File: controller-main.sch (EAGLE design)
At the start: 24 parts

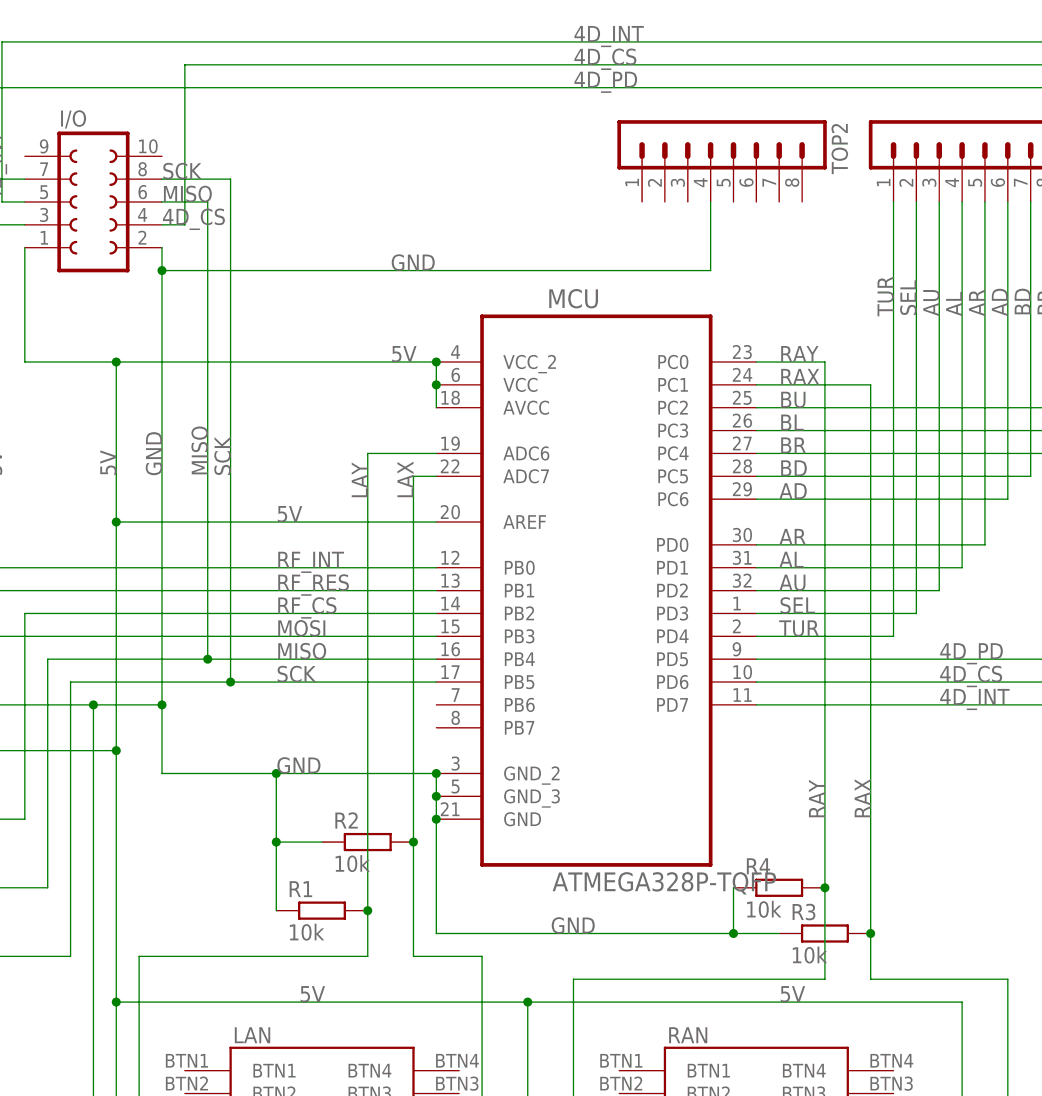
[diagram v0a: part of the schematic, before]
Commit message: Created basic main board desing
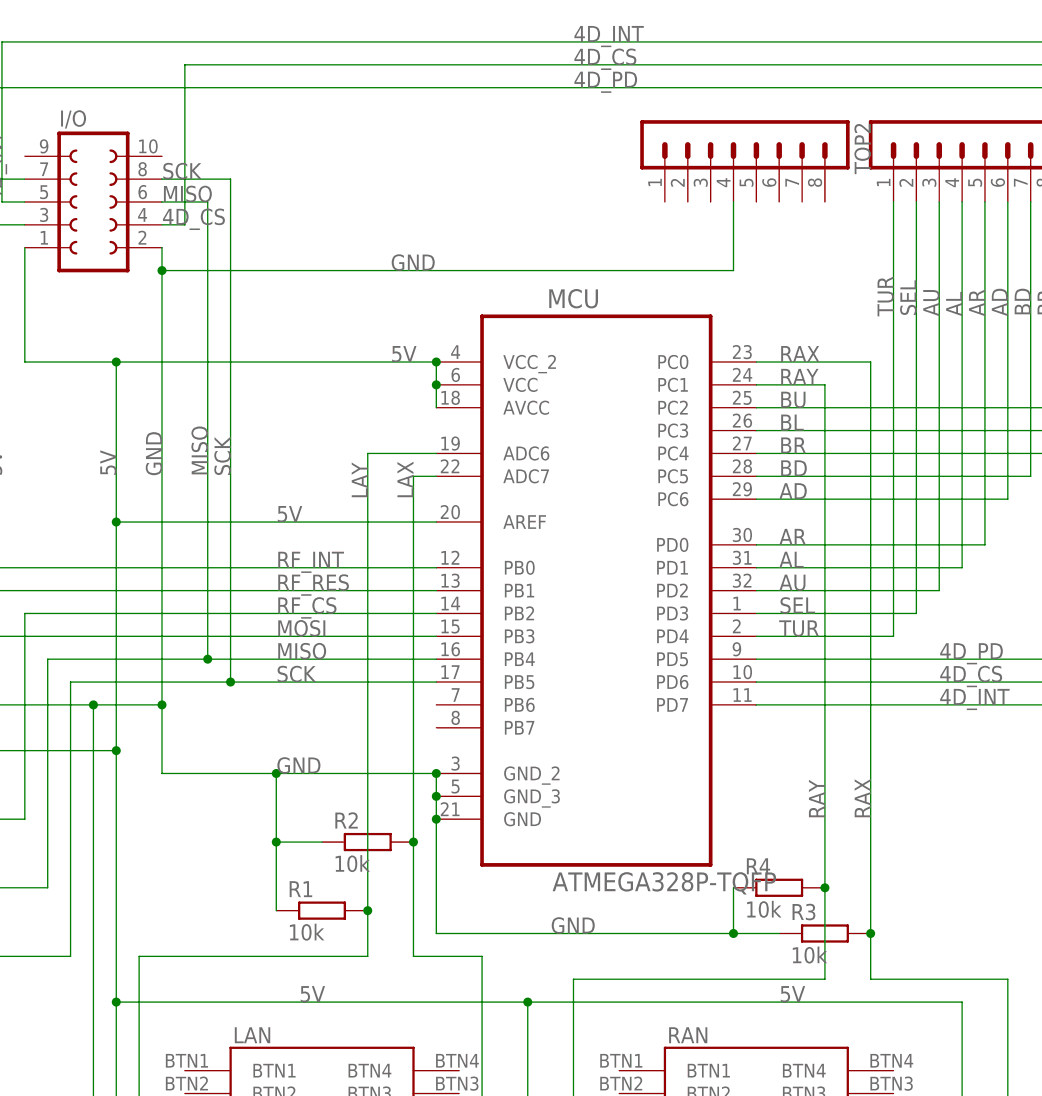
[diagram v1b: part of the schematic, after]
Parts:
- TOP2: device con-lstb:MA08-1 -> con-lstb:MA08-1W
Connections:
- net RAX: now also MCU.PC0; no longer MCU.PC1
- net RAY: now also MCU.PC1; no longer MCU.PC0
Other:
- moved on the sheet: TOP2
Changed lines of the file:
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@@
 <?xml version="1.0" encoding="utf-8"?>
 <!DOCTYPE eagle SYSTEM "eagle.dtd">
-<eagle version="8.4.0">
+<eagle version="8.4.1">
 <drawing>
 <settings>
@@
 <part name="I/O" library="con-lsta" library_urn="urn:adsk.eagle:library:161" deviceset="FE05-2W" device="" package3d_urn="urn:adsk.eagle:package:8205/1"/>
 <part name="TOP1" library="con-lstb" library_urn="urn:adsk.eagle:library:162" deviceset="MA10-1W" device="" package3d_urn="urn:adsk.eagle:package:8347/1"/>
-<part name="TOP2" library="con-lstb" library_urn="urn:adsk.eagle:library:162" deviceset="MA08-1" device="" package3d_urn="urn:adsk.eagle:package:8343/1"/>
 <part name="LAN" library="joystick" deviceset="JOYSTICK" device="JOYSTICKWBTN" value="JOYSTICK"/>
 <part name="RAN" library="joystick" deviceset="JOYSTICK" device="JOYSTICKWBTN" value="JOYSTICK"/>
@@
 <part name="R15" library="resistor" library_urn="urn:adsk.eagle:library:348" deviceset="R-EU_" device="M1206" package3d_urn="urn:adsk.eagle:package:26088/1" value="2k"/>
 <part name="R16" library="resistor" library_urn="urn:adsk.eagle:library:348" deviceset="R-EU_" device="M1206" package3d_urn="urn:adsk.eagle:package:26088/1" value="1k"/>
+<part name="TOP2" library="con-lstb" library_urn="urn:adsk.eagle:library:162" deviceset="MA08-1W" device="" package3d_urn="urn:adsk.eagle:package:8344/1"/>
 </parts>
 <sheets>
@@
 <instance part="I/O" gate="G$1" x="81.28" y="121.92"/>
 <instance part="TOP1" gate="1" x="180.34" y="129.54" rot="R270"/>
-<instance part="TOP2" gate="1" x="149.86" y="129.54" rot="R270"/>
 <instance part="LAN" gate="G$1" x="106.68" y="17.78"/>
 <instance part="RAN" gate="G$1" x="154.94" y="17.78"/>
@@
 <instance part="R15" gate="G$1" x="45.72" y="38.1"/>
 <instance part="R16" gate="G$1" x="55.88" y="38.1"/>
+<instance part="TOP2" gate="1" x="152.4" y="129.54" rot="R270"/>
 </instances>
 <busses>
@@
 <wire x1="88.9" y1="114.3" x2="88.9" y2="116.84" width="0.1524" layer="91"/>
 <junction x="88.9" y="66.04"/>
-<pinref part="TOP2" gate="1" pin="4"/>
 <wire x1="40.64" y1="66.04" x2="81.28" y2="66.04" width="0.1524" layer="91"/>
 <wire x1="81.28" y1="66.04" x2="88.9" y2="66.04" width="0.1524" layer="91"/>
-<wire x1="149.86" y1="121.92" x2="149.86" y2="114.3" width="0.1524" layer="91"/>
-<wire x1="149.86" y1="114.3" x2="88.9" y2="114.3" width="0.1524" layer="91"/>
 <junction x="88.9" y="114.3"/>
 <pinref part="LAN" gate="G$1" pin="GNDY"/>
+<wire x1="152.4" y1="114.3" x2="88.9" y2="114.3" width="0.1524" layer="91"/>
 <wire x1="81.28" y1="66.04" x2="81.28" y2="10.16" width="0.1524" layer="91"/>
 <wire x1="81.28" y1="10.16" x2="91.44" y2="10.16" width="0.1524" layer="91"/>
@@
 <wire x1="25.4" y1="60.96" x2="25.4" y2="58.42" width="0.1524" layer="91"/>
 <junction x="25.4" y="60.96"/>
+<pinref part="TOP2" gate="1" pin="4"/>
+<wire x1="152.4" y1="121.92" x2="152.4" y2="114.3" width="0.1524" layer="91"/>
 </segment>
 </net>
@@
 <net name="RAY" class="0">
 <segment>
-<pinref part="MCU" gate="A" pin="PC0"/>
-<wire x1="162.56" y1="104.14" x2="154.94" y2="104.14" width="0.1524" layer="91"/>
-<wire x1="162.56" y1="104.14" x2="162.56" y2="45.72" width="0.1524" layer="91"/>
+<wire x1="162.56" y1="101.6" x2="162.56" y2="45.72" width="0.1524" layer="91"/>
 <wire x1="134.62" y1="35.56" x2="162.56" y2="35.56" width="0.1524" layer="91"/>
 <pinref part="R4" gate="G$1" pin="2"/>
 <junction x="162.56" y="45.72"/>
-<label x="157.48" y="104.14" size="1.778" layer="95"/>
+<label x="157.48" y="101.6" size="1.778" layer="95"/>
 <label x="162.56" y="53.34" size="1.778" layer="95" rot="R90"/>
 <pinref part="RAN" gate="G$1" pin="OUTY"/>
@@
 <wire x1="134.62" y1="12.7" x2="134.62" y2="35.56" width="0.1524" layer="91"/>
 <wire x1="162.56" y1="35.56" x2="162.56" y2="45.72" width="0.1524" layer="91"/>
+<pinref part="MCU" gate="A" pin="PC1"/>
+<wire x1="154.94" y1="101.6" x2="162.56" y2="101.6" width="0.1524" layer="91"/>
 </segment>
 </net>
 <net name="RAX" class="0">
 <segment>
-<pinref part="MCU" gate="A" pin="PC1"/>
-<wire x1="154.94" y1="101.6" x2="167.64" y2="101.6" width="0.1524" layer="91"/>
-<wire x1="167.64" y1="101.6" x2="167.64" y2="40.64" width="0.1524" layer="91"/>
+<wire x1="167.64" y1="104.14" x2="167.64" y2="40.64" width="0.1524" layer="91"/>
 <pinref part="R3" gate="G$1" pin="2"/>
 <wire x1="167.64" y1="40.64" x2="167.64" y2="35.56" width="0.1524" layer="91"/>
@@
 <wire x1="182.88" y1="35.56" x2="182.88" y2="12.7" width="0.1524" layer="91"/>
 <wire x1="182.88" y1="12.7" x2="170.18" y2="12.7" width="0.1524" layer="91"/>
-<label x="157.48" y="101.6" size="1.778" layer="95"/>
+<label x="157.48" y="104.14" size="1.778" layer="95"/>
 <label x="167.64" y="53.34" size="1.778" layer="95" rot="R90"/>
-</segment>
-</net>
+<pinref part="MCU" gate="A" pin="PC0"/>
+<wire x1="154.94" y1="104.14" x2="167.64" y2="104.14" width="0.1524" layer="91"/>
+</segment>
+</net>

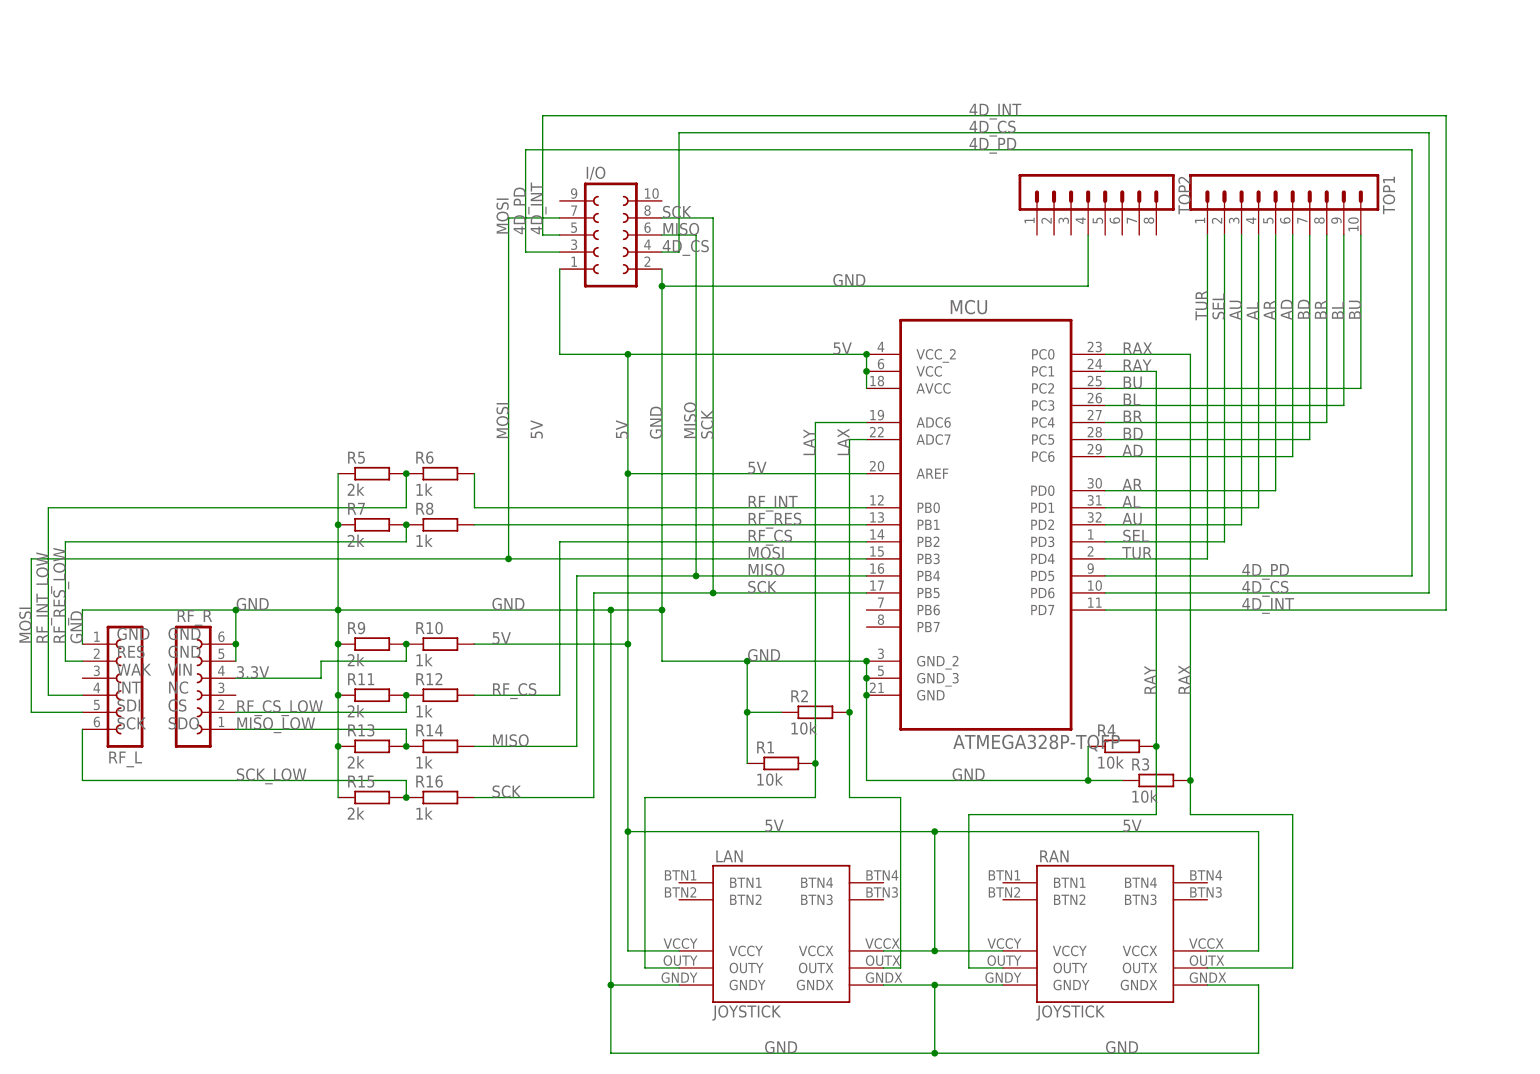
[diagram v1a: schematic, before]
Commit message: Changed pin connections on the main board
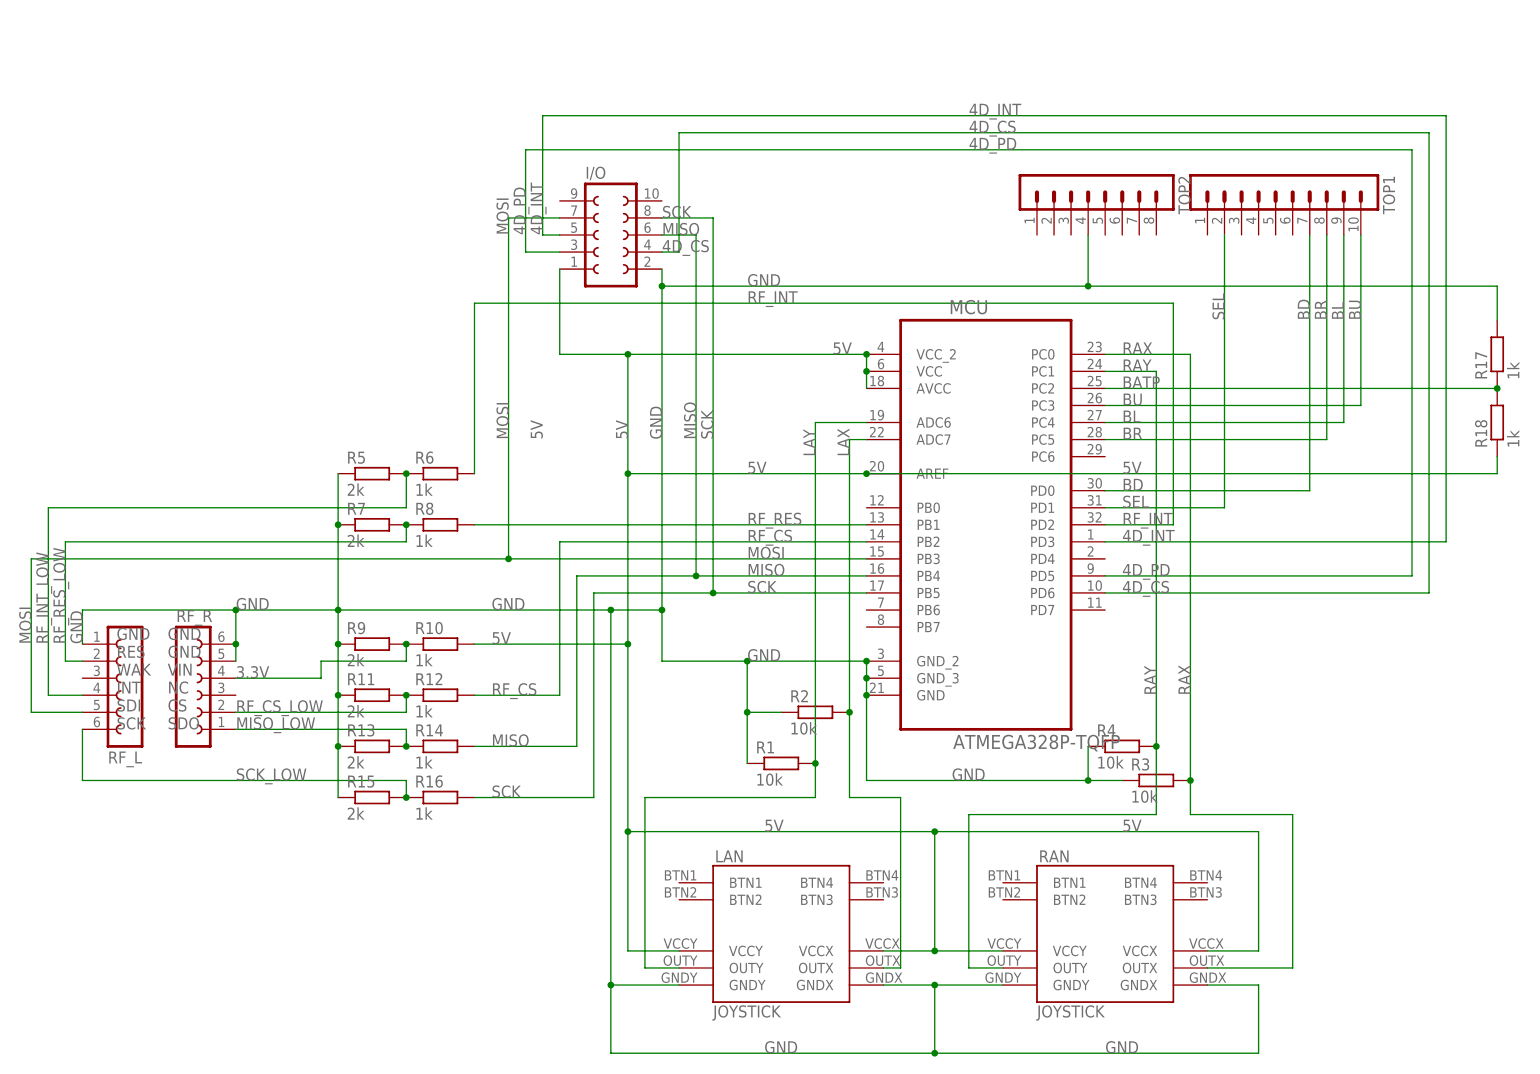
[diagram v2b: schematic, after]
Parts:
- added R17, R18: 1k, resistor:R-EU_M1206
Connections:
- removed net AD: MCU.PC6, TOP1.6
- removed net AL: MCU.PD1, TOP1.4
- removed net AR: MCU.PD0, TOP1.5
- removed net AU: MCU.PD2, TOP1.3
- removed net TUR: MCU.PD4, TOP1.1
- new net BATP: MCU.PC2, R17.1, R18.2
- net 4D_INT: now also MCU.PD3; no longer MCU.PD7
- net 5V: now also R18.1
- net BD: now also MCU.PD0; no longer MCU.PC5
- net BL: now also MCU.PC4; no longer MCU.PC3
- net BR: now also MCU.PC5; no longer MCU.PC4
- net BU: now also MCU.PC3; no longer MCU.PC2
- net GND: now also R17.2
- net RF_INT: now also MCU.PD2; no longer MCU.PB0
- net SEL: now also MCU.PD1; no longer MCU.PD3

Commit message: only half done
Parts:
- removed R10, R12, R14, R16, R17, R18, R6, R8: 1k, resistor:R-EU_M1206
- removed R11, R13, R15, R5, R7, R9: 2k, resistor:R-EU_M1206
- removed TOP1: (no value), con-lstb:MA10-1W
- removed TOP2: (no value), con-lstb:MA08-1W
- added C1: (no value), resistor:C-EUC1206
- added IC1: REG1117, burr-brown:REG1117
- added SV1: (no value), con-lstb:MA03-1
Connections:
- removed net 4D_INT: I/O.5, MCU.PD3
- removed net BATP: MCU.PC2, R17.1, R18.2
- removed net BL: MCU.PC4, TOP1.9
- removed net BR: MCU.PC5, TOP1.8
- removed net BU: MCU.PC3, TOP1.10
- removed net MISO_LOW: R13.2, R14.1, RF_R.1
- removed net RF_CS_LOW: R11.2, R12.1, RF_R.2
- removed net RF_INT_LOW: R5.2, R6.1, RF_L.4
- removed net RF_RES_LOW: R7.2, R8.1, RF_L.2
- removed net SCK_LOW: R15.2, R16.1, RF_L.6
- net 3.3V: now also IC1.VOUT; no longer R10.1, R9.2
- net 4D_CS: now also I/O.5, MCU.PB0; no longer I/O.4, MCU.PD6
- net 4D_PD: now also MCU.PD7; no longer MCU.PD5
- net 5V: now also C1.1, IC1.VIN; no longer R10.2, R18.1
- net BD: now also MCU.PD5, SV1.3; no longer MCU.PD0, TOP1.7
- net GND: now also C1.2, IC1.GND, SV1.1; no longer R11.1, R13.1, R15.1, R17.2, R5.1, R7.1, R9.1, TOP2.4
- net LAX: now also MCU.PC3; no longer MCU.ADC7
- net LAY: now also MCU.PC2; no longer MCU.ADC6
- net MISO: now also RF_R.1; no longer R14.2
- net RAX: now also MCU.PC5; no longer MCU.PC0
- net RAY: now also MCU.PC4; no longer MCU.PC1
- net RF_CS: now also RF_R.2; no longer R12.2
- net RF_INT: now also MCU.PD3, RF_L.4; no longer MCU.PD2, R6.2
- net RF_RES: now also RF_L.2; no longer R8.2
- net SCK: now also RF_L.6; no longer R16.2
- net SEL: now also MCU.PD6, SV1.2; no longer MCU.PD1, TOP1.2

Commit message: finished the main board
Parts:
- added R5, R6, R7, R8, R9: (no value), resistor:R-EU_M1206
- R1, R2, R3, R4: value 10k -> (none)
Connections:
- new net 5V2: R2.2, R6.2, RAN.VCCX
- new net 5V_R: R2.1, RAN.VCCY
- new net GND_R: LAN.GNDX, LAN.GNDY, R1.2, RAN.GNDX, RAN.GNDY
- new net MISO2: I/O.6, R3.2
- new net MISO3: MCU.PB4, R4.2
- new net N$1: R1.1, R5.2
- new net N$2: LAN.OUTX, R9.1
- new net RST: MCU.PC6, R7.2
- new net RST2: R7.1, R8.2
- new net RST3: I/O.4, R8.1
- net 5V: now also R6.1; no longer RAN.VCCX, RAN.VCCY
- net GND: now also R5.1; no longer LAN.GNDX, LAN.GNDY, R1.1, R2.1, R3.1, R4.1, RAN.GNDX, RAN.GNDY
- net LAX: now also R9.2; no longer LAN.OUTX, R2.2
- net LAY: no longer R1.2
- net MISO: now also R3.1, R4.1; no longer I/O.6, MCU.PB4
- net RAX: no longer R3.2
- net RAY: no longer R4.2
- net RF_CS: now also MCU.PC0; no longer MCU.PB2
- net RF_RES: now also MCU.PC1; no longer MCU.PB1
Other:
- moved on the sheet: R1, R2, R3, R4
